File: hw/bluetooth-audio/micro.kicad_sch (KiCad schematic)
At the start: 19 parts, among them J6 2x5 JTAG header, U2 IS2083BM-232

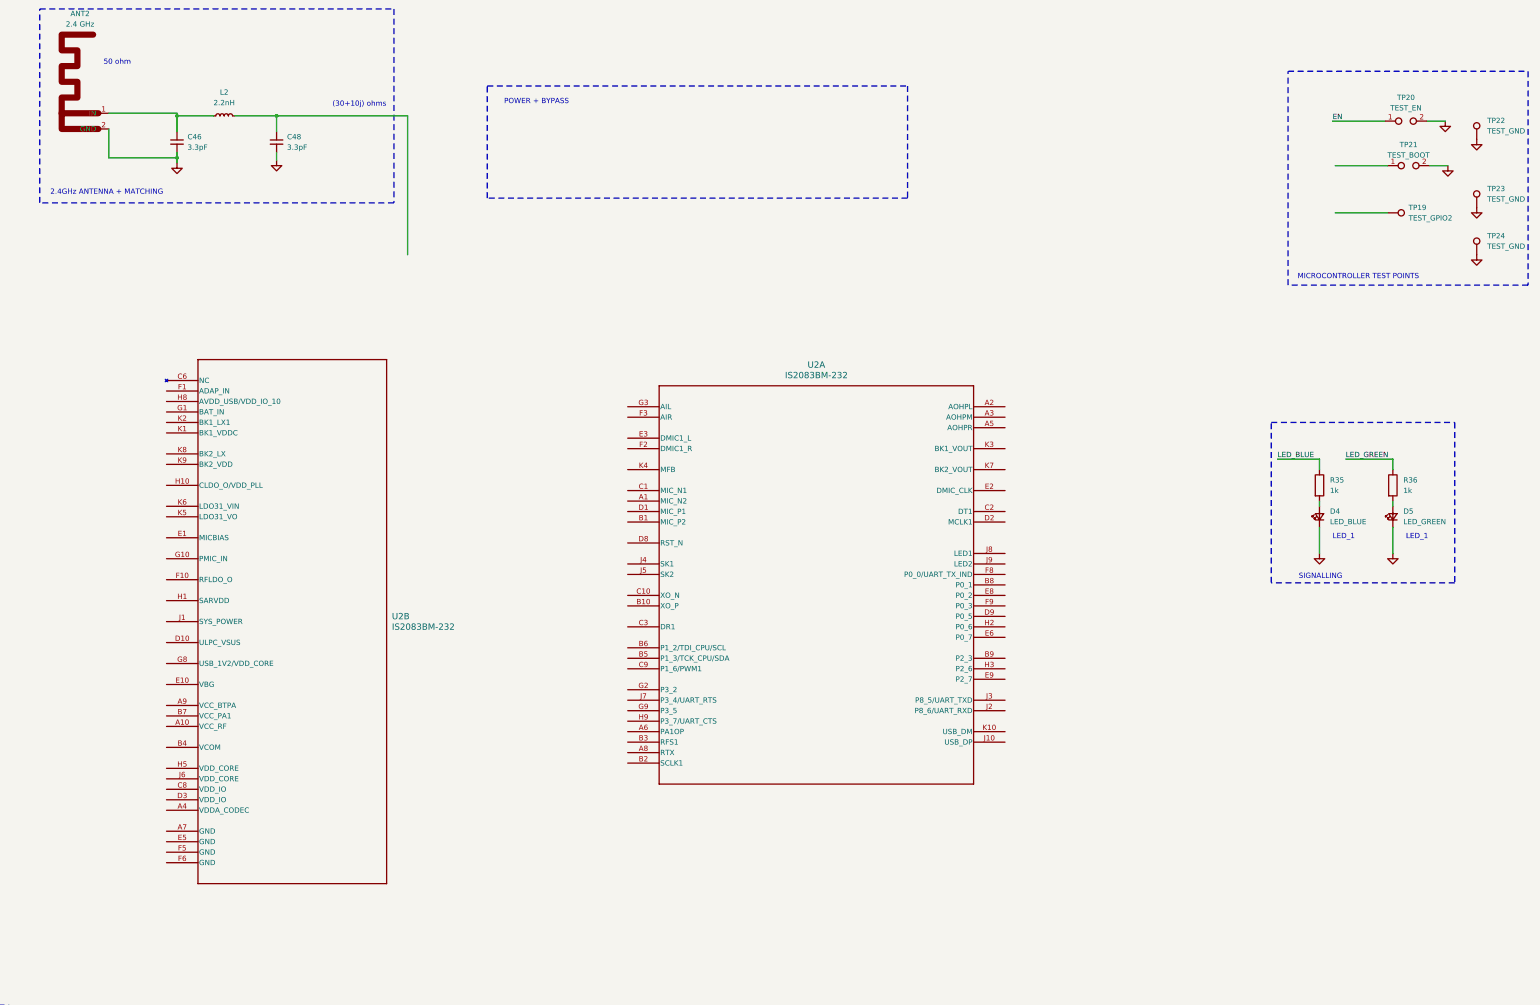
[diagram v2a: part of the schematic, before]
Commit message: All decoupling caps and labels on IS2083
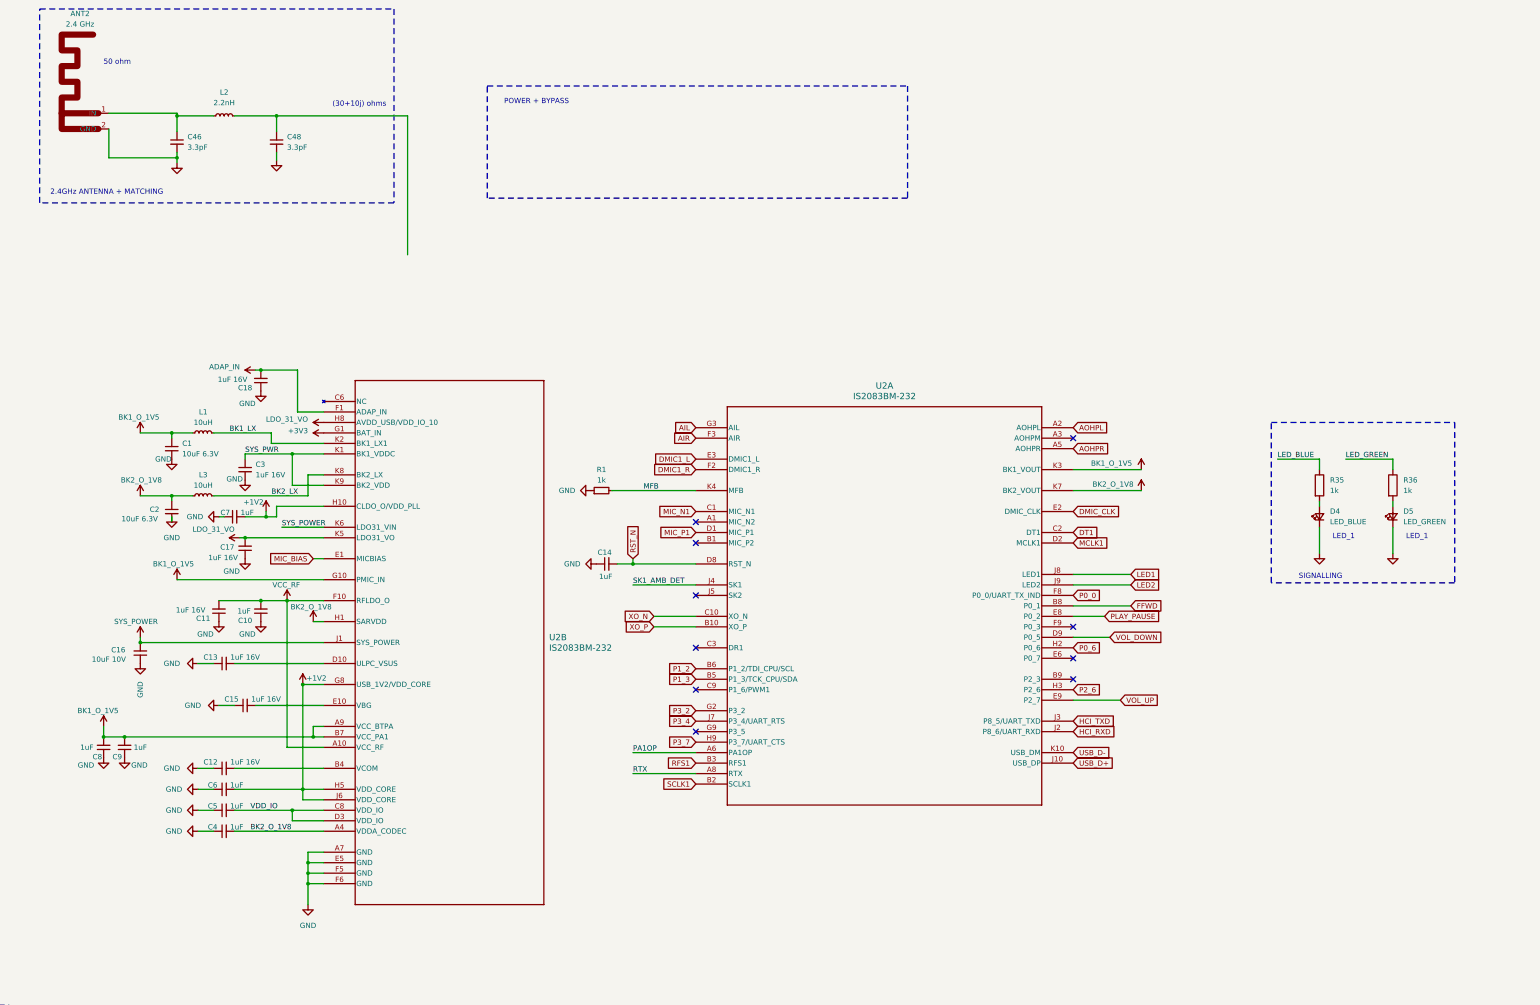
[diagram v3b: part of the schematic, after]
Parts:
- removed TP19: TEST_GPIO2, TestPoint:TestPoint_Pad_D1.0mm, symbol Connector:TestPoint
- removed TP20: TEST_EN, custom_footprints:TestPoint_Pad_2x1_D1.0mm, symbol Connector:TestPoint_2Pole
- removed TP21: TEST_BOOT, custom_footprints:TestPoint_Pad_2x1_D1.0mm, symbol Connector:TestPoint_2Pole
- removed TP22, TP23, TP24: TEST_GND, TestPoint:TestPoint_Pad_D1.0mm, symbol Connector:TestPoint
- added C1, C2: 10uF 6.3V, Capacitor_SMD:C_0603_1608Metric, symbol Device:C_Small
- added C10, C14, C4, C5, C6, C7, C8, C9: 1uF, Capacitor_SMD:C_0402_1005Metric, symbol Device:C_Small
- added C11, C12, C13, C15, C17, C18: 1uF 16V, Capacitor_SMD:C_0603_1608Metric, symbol Device:C_Small
- added C16: 10uF 10V, Capacitor_SMD:C_0603_1608Metric, symbol Device:C_Small
- added C3: 1uF 16V, Capacitor_SMD:C_0402_1005Metric, symbol Device:C_Small
- added L1, L3: 10uH, Inductor_SMD:L_0805_2012Metric, symbol Device:L_Small
- added R1: 1k, Resistor_SMD:R_0402_1005Metric, symbol Device:R_Small
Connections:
- net +3V3: now also U2.G1 (BAT_IN)
- net GND: now also U2.A7 (GND), U2.E5 (GND), U2.F5 (GND), U2.F6 (GND), C1.2, C10.1, C11.1, C12.1, C13.1, C14.1, C15.1, C16.1, C17.1, C18.1, C2.2, C3.2, C4.1, C5.1, C6.1, C7.1, C8.1, C9.1, R1.1
- net AOHPL: now reaches U2.A2 (AOHPL)
- net AOHPR: now reaches U2.A5 (AOHPR)
- net PA1OP: now reaches U2.A6 (PA1OP)
- net RTX: now reaches U2.A8 (RTX)
- net XO_P: now reaches U2.B10 (XO_P)
- net SCLK1: now reaches U2.B2 (SCLK1)
- net RFS1: now reaches U2.B3 (RFS1)
- net P1_3: now reaches U2.B5 (P1_3/TCK_CPU/SDA)
- net P1_2: now reaches U2.B6 (P1_2/TDI_CPU/SCL)
- net FFWD: now reaches U2.B8 (P0_1)
- net MIC_N1: now reaches U2.C1 (MIC_N1)
- net XO_N: now reaches U2.C10 (XO_N)
- net DT1: now reaches U2.C2 (DT1)
- net MIC_P1: now reaches U2.D1 (MIC_P1)
- net MCLK1: now reaches U2.D2 (MCLK1)
- net RST_N: now reaches U2.D8 (RST_N)
- net RST_N: now also C14.2
- net VOL_DOWN: now reaches U2.D9 (P0_5)
- net DMIC_CLK: now reaches U2.E2 (DMIC_CLK)
- net DMIC1_L: now reaches U2.E3 (DMIC1_L)
- net PLAY_PAUSE: now reaches U2.E8 (P0_2)
- net VOL_UP: now reaches U2.E9 (P2_7)
- net DMIC1_R: now reaches U2.F2 (DMIC1_R)
- net AIR: now reaches U2.F3 (AIR)
- net P0_0: now reaches U2.F8 (P0_0/UART_TX_IND)
- net P3_2: now reaches U2.G2 (P3_2)
- net AIL: now reaches U2.G3 (AIL)
- net P0_6: now reaches U2.H2 (P0_6)
- net P2_6: now reaches U2.H3 (P2_6)
- net P3_7: now reaches U2.H9 (P3_7/UART_CTS)
- net USB_D+: now reaches U2.J10 (USB_DP)
- net HCI_RXD: now reaches U2.J2 (P8_6/UART_RXD)
- net HCI_TXD: now reaches U2.J3 (P8_5/UART_TXD)
- net SK1_AMB_DET: now reaches U2.J4 (SK1)
- net P3_4: now reaches U2.J7 (P3_4/UART_RTS)
- net LED1: now reaches U2.J8 (LED1)
- net LED2: now reaches U2.J9 (LED2)
- net USB_D-: now reaches U2.K10 (USB_DM)
- net BK1_O_1V5: now reaches U2.K3 (BK1_VOUT)
- net BK1_O_1V5: now also U2.A9 (VCC_BTPA), U2.B7 (VCC_PA1), U2.G10 (PMIC_IN), C1.1, C8.2, C9.2, L1.1
- net MFB: now reaches U2.K4 (MFB)
- net MFB: now also R1.2
- net BK2_O_1V8: now reaches U2.K7 (BK2_VOUT)
- net BK2_O_1V8: now also U2.A4 (VDDA_CODEC), U2.H1 (SARVDD), C2.1, C4.2, L3.1
- net VCC_RF: now reaches U2.A10 (VCC_RF)
- net VCC_RF: now also U2.F10 (RFLDO_O), C10.2, C11.2
- net at U2.B4 (VCOM): now also C12.2
- net VDD_IO: now reaches U2.C8 (VDD_IO)
- net VDD_IO: now also U2.D3 (VDD_IO), C5.2
- net at U2.D10 (ULPC_VSUS): now also C13.2
- net MIC_BIAS: now reaches U2.E1 (MICBIAS)
- net at U2.E10 (VBG): now also C15.2
- net ADAP_IN: now reaches U2.F1 (ADAP_IN)
- net ADAP_IN: now also C18.2
- net +1V2: now reaches U2.G8 (USB_1V2/VDD_CORE)
- net +1V2: now also U2.H10 (CLDO_O/VDD_PLL), U2.H5 (VDD_CORE), U2.J6 (VDD_CORE), C6.2, C7.2
- net LDO_31_VO: now reaches U2.H8 (AVDD_USB/VDD_IO_10)
- net LDO_31_VO: now also U2.K5 (LDO31_VO), C17.2
- net SYS_POWER: now reaches U2.J1 (SYS_POWER)
- net SYS_POWER: now also U2.K6 (LDO31_VIN), C16.2
- net SYS_PWR: now reaches U2.K1 (BK1_VDDC)
- net SYS_PWR: now also U2.K9 (BK2_VDD), C3.1
- net BK1_LX: now reaches U2.K2 (BK1_LX1)
- net BK1_LX: now also L1.2
- net BK2_LX: now reaches U2.K8 (BK2_LX)
- net BK2_LX: now also L3.2
- no-connect marks 1 -> 11
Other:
- note removed: "MICROCONTROLLER TEST POINTS"
- moved on the sheet: U2A, U2B

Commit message: TODO diff
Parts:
- removed D5: LED_GREEN, LED_SMD:LED_0805_2012Metric, symbol Device:LED_Small
- removed R35, R36: 1k, Resistor_SMD:R_0402_1005Metric, symbol Device:R
- added C21: 100nF, Capacitor_SMD:C_0402_1005Metric, symbol Device:C_Small
- added C22, C23: 10pF, Capacitor_SMD:C_0402_1005Metric, symbol Device:C_Small
- added D6: LED_GREEN, LED_SMD:LED_0805_2012Metric, symbol Device:LED_Small
- added R7: 0R, Resistor_SMD:R_0402_1005Metric, symbol Device:R
- added Y1: TSX-3225 16.0000MF18X-AC0, Crystal:Crystal_SMD_SeikoEpson_TSX3225-4Pin_3.2x2.5mm, symbol Device:Crystal_GND24
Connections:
- net GND: now also C21.1, C22.1, C23.1, Y1.2, Y1.4; no longer D4.1 (K)
- net LDO_31_VO: now also R7.1
- net LED1: now also D4.1 (K)
- net LED2: now also D6.1 (K)
- net SYS_POWER: now also D4.2 (A), C21.2, D6.2 (A)
- net VDD_IO: now also R7.2
- net XO_N: now also C23.2, Y1.3
- net XO_P: now also C22.2, Y1.1
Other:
- note added: "1.28V RF LDO output"
- note added: "1.2V ULPC PWR out max 1mA"
- note added: "1.2V core PWR input"
- note added: "1V5 Buck FB path"
- note added: "1V8 Buck FB path"
- note added: "1V8?? PWR in for internal blocks"
- note added: "3V LDO input"
- note added: "3V LDO output for VDD_IO power"
- note added: "5V input for battery charging"
- note added: "AUX JACK DETECT"
- note added: "Bandgap output ref"
- note added: "Codec PWR in (1.8V)"
- note added: "Codec biasing voltage Connect 4u7 F to gnd"
- note added: "Core 1V2 LDO output"
- note added: "Core 1V2 PWR input"
- note added: "EXT AUDIO AMP EN"
- note added: "FWD"
- note added: "I/O PWR supply input (Connect to LDO31_VO)"
- note added: "Input PWR from battery"
- note added: "JTAG EMUC CPU"
- note added: "JTAG EMUD CPU"
- note added: "MFB/PWR"
- note added: "Microphone bias voltage"
- note added: "PAIRING"
- note added: "PLAY/PAUSE"
- note added: "PWR (1.28V) for RF synth, RX/TX"
- note added: "PWR for MPA"
- note added: "PWR for RF amp"
- note added: "PWR input for 1V5 buck"
- note added: "PWR input for 1V8 buck"
- note added: "Pwr for USB peripheral (from LDO)"
- note added: "REV"
- note added: "SAR ADC 1V8 input"
- note added: "System PWR output (from ADAP_IN / BAT_IN)"
- note added: "VOL+"
- note added: "VOL-"
- note removed: "LED_1"
- note removed: "SIGNALLING"
- moved on the sheet: C1, C10, C11, C12, C13, C14, C15, C16, C17, C18, C2, C3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
